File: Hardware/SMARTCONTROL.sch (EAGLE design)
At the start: 37 parts, among them IC1 ESP12-SMT, Q2 RJU003N03, Q3 RJU003N03, Q4 RJU003N03, Q5 RJU003N03

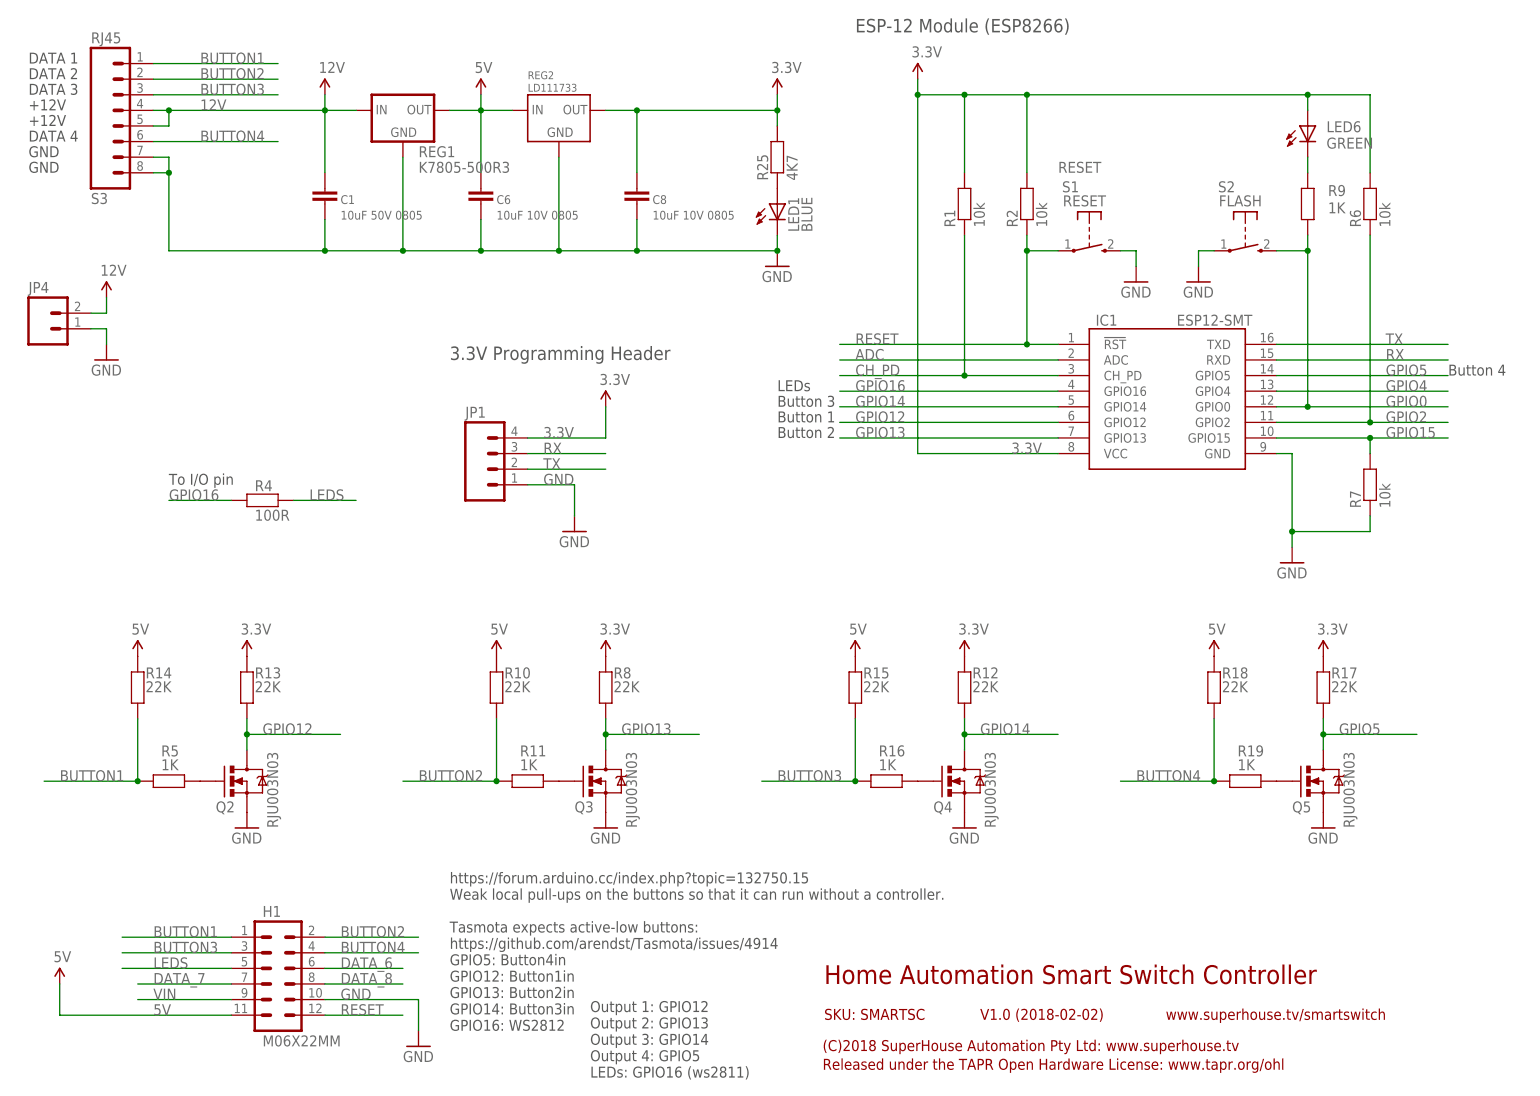
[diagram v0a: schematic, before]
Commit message: Replaced 3.3V regulator. Switched button1 and LED pins. Extended PCB to improve bolt clearance. Changed bottom layer to 3.3V.
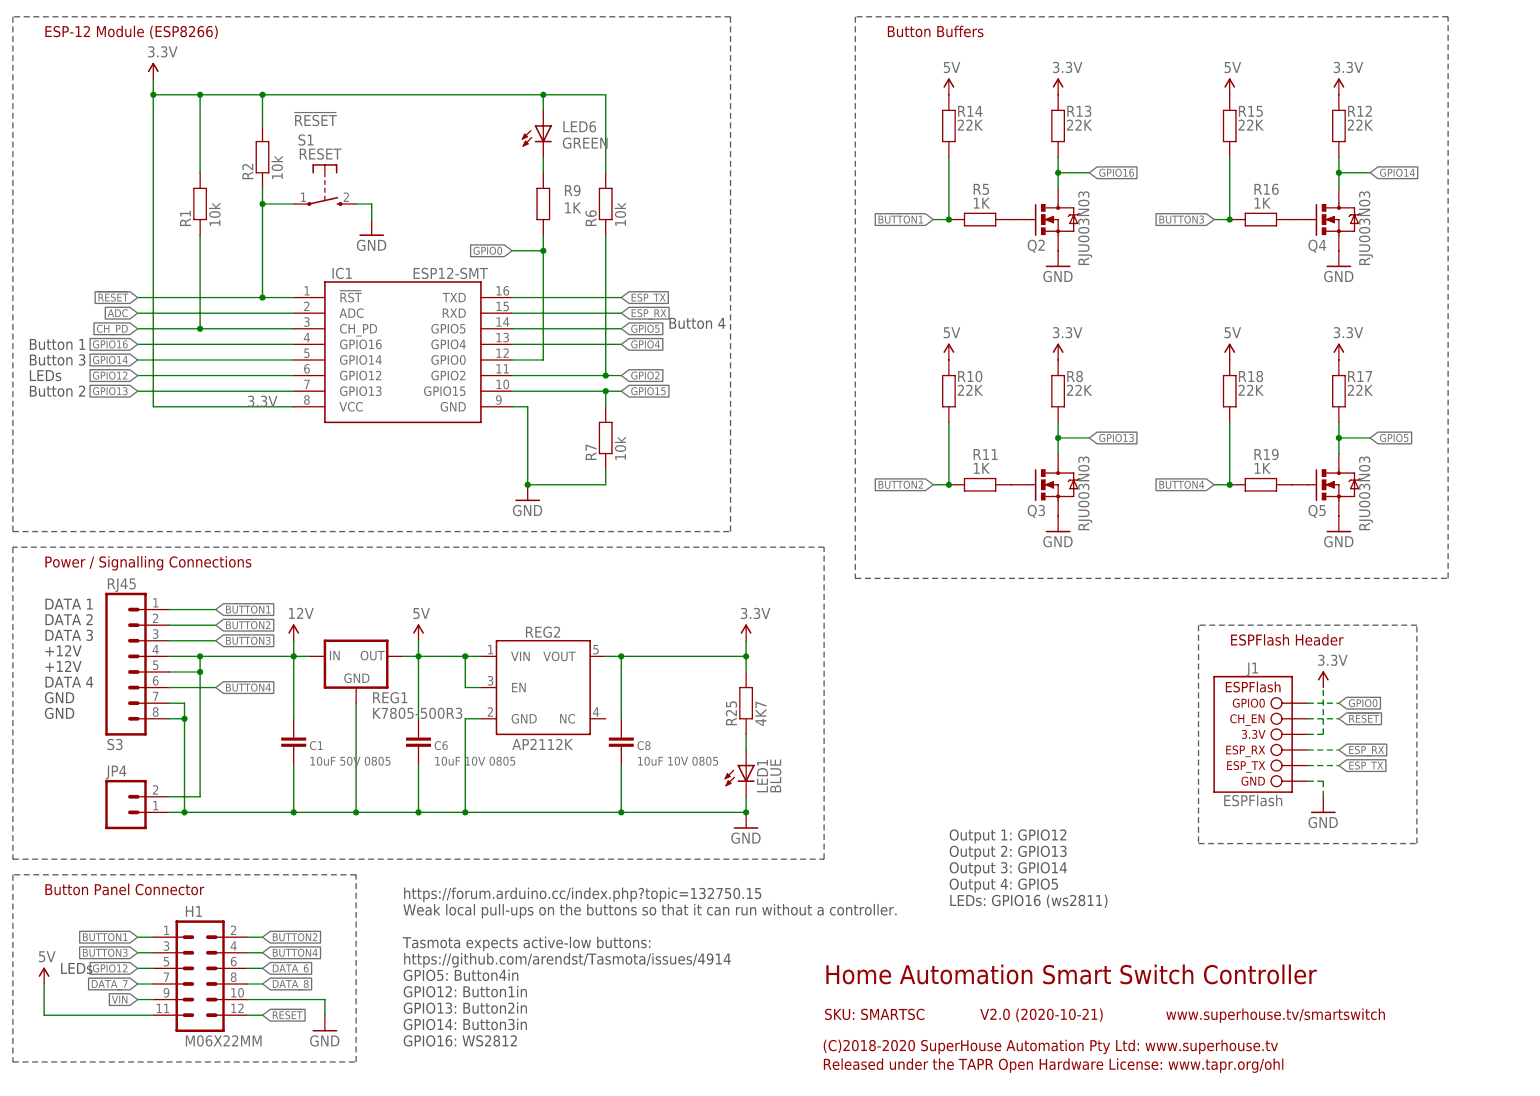
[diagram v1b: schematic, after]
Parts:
- removed JP1: (no value), freetronics-jon:M04PTH
- removed R4: 100R, SuperHouse-DiscreteSemi:RESISTOR0603
- removed S2: FLASH, SuperHouse-Switches:TAC_SWITCH_2PINSMT
- added J1: ESPFLASH-1X6-2.54-SOCKET, SuperHouse-ESPFlash:ESPFLASH-1X6-2.54-SOCKET
- JP4: device freetronics-jon:M023.5MM -> SuperHouse-Connectors:M02-SCREW-5MM
- REG2: value LD111733 -> AP2112KSOT25; device SuperHouse-Regulators:LD1117 -> SuperHouse-Regulators:AP2112KSOT25
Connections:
- removed net LEDS: H1.5, R4.1
- removed net RESET: H1.12, IC1.!RST, R2.1, S1.P
- removed net RX: IC1.RXD, JP1.3
- removed net TX: IC1.TXD, JP1.2
- new net !RESET: H1.12, IC1.!RST, J1.CH_EN, R2.1, S1.P
- new net ESP_RX: IC1.RXD, J1.ESP_RX
- new net ESP_TX: IC1.TXD, J1.ESP_TX
- net 3.3V: now also J1.3.3V, REG2.VOUT; no longer JP1.4, REG2.OUT
- net 5V: now also REG2.EN, REG2.VIN; no longer REG2.IN
- net GND: now also J1.GND; no longer JP1.1, S2.P
- net GPIO0: now also J1.GPIO0; no longer S2.S
- net GPIO12: now also H1.5; no longer Q2.D, R13.1
- net GPIO16: now also Q2.D, R13.1; no longer R4.2
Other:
- note added: "(C)2018-2020 SuperHouse Automation Pty Ltd: www.superhouse.tv"
- note added: "Button Buffers"
- note added: "Button Panel Connector"
- note added: "ESPFlash Header"
- note added: "Power / Signalling Connections"
- note added: "V2.0 (2020-10-21)"
- note removed: "(C)2018 SuperHouse Automation Pty Ltd: www.superhouse.tv"
- note removed: "3.3V Programming Header"
- note removed: "SOT-223"
- note removed: "To I/O pin"
- note removed: "V1.0 (2018-02-02)"
- moved on the sheet: C1, C6, C8, H1, IC1, JP4, LED1, LED6, Q2, Q3, Q4, Q5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

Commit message: Routing for expanded PCB.
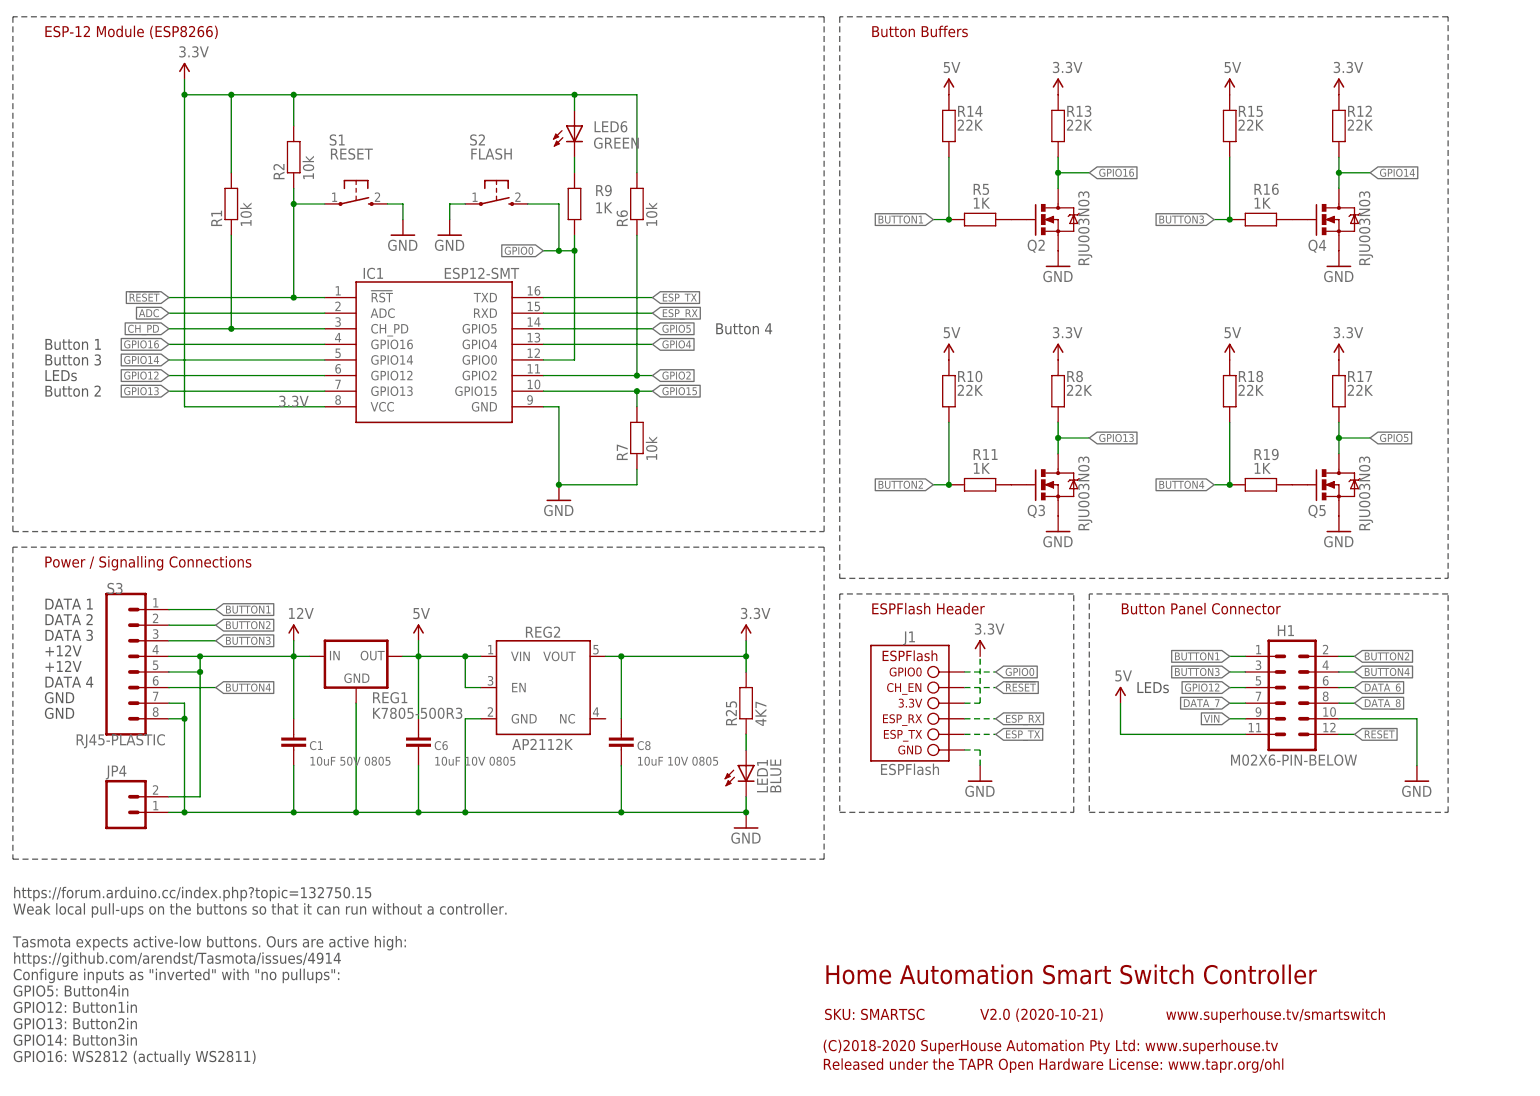
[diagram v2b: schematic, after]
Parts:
- added S2: FLASH, SuperHouse-Switches:TAC_SWITCH_2PINSMT
- H1: value M06X22MM -> M02X6-PIN-BELOW; device freetronics-jon:M06X22MM -> SuperHouse-Connectors:M02X6-PIN-BELOW
- REG1: device SuperHouse-Regulators:K78XX-500R3 -> SuperHouse-Regulators:78XX-K78XX-VERTICAL
- S3: value RJ45 -> RJ45-PLASTIC; device SuperHouse-Connectors:RJ45 -> SuperHouse-Connectors:RJ45-PLASTIC
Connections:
- net GND: now also S2.P
- net GPIO0: now also S2.S
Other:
- note added: "https://forum.arduino.cc/index.php?topic=132750.15 Weak local pull-ups on the buttons so that it can run without a controller. Tasmota expects active-low buttons. Ours are active high: https://github.com/arendst/Tasmota/issues/4914 Configure inputs as "inverted" with "no pullups": GPIO5: Button4in GPIO12: Button1in GPIO13: Button2in GPIO14: Button3in GPIO16: WS2812 (actually WS2811)"
- note removed: "Output 1: GPIO12 Output 2: GPIO13 Output 3: GPIO14 Output 4: GPIO5 LEDs: GPIO16 (ws2811)"
- note removed: "https://forum.arduino.cc/index.php?topic=132750.15 Weak local pull-ups on the buttons so that it can run without a controller. Tasmota expects active-low buttons: https://github.com/arendst/Tasmota/issues/4914 GPIO5: Button4in GPIO12: Button1in GPIO13: Button2in GPIO14: Button3in GPIO16: WS2812"
- moved on the sheet: IC1, J1, LED6, R1, R2, R6, R7, R9
